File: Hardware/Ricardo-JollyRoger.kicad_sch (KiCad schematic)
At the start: 46 parts, among them J1 RBUS, J3 Conn_01x08_Pin, U1 ESP32-S3, U7 LM66200DRLR, Y1 R940000171

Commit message: Updated footprints
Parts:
- 12VLED1, 3V3LED1, CRXLED1, CTXLED1, TXLED1: footprint Resistor_SMD:R_0402_1005Metric -> LED_SMD:LED_0402_1005Metric
- U7: footprint SOTFL50P160X60-8N -> iclr:SOTFL50P160X60-8N
- Y1: footprint Crystal:Crystal_SMD_2016-4Pin_2.0x1.6mm -> iclr:Crystal_SMD_2016-4Pin_2.0x1.6mm
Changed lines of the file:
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@@
 			)
 		)
-		(property "Footprint" "Resistor_SMD:R_0402_1005Metric"
+		(property "Footprint" "LED_SMD:LED_0402_1005Metric"
 			(at 25.4 21.59 90)
 			(effects
@@
 			)
 		)
-		(property "Footprint" "Resistor_SMD:R_0402_1005Metric"
+		(property "Footprint" "LED_SMD:LED_0402_1005Metric"
 			(at 54.61 21.59 90)
 			(effects
@@
 			)
 		)
-		(property "Footprint" "Resistor_SMD:R_0402_1005Metric"
+		(property "Footprint" "LED_SMD:LED_0402_1005Metric"
 			(at 63.5 26.67 90)
 			(effects
@@
 			)
 		)
-		(property "Footprint" "Resistor_SMD:R_0402_1005Metric"
+		(property "Footprint" "LED_SMD:LED_0402_1005Metric"
 			(at 25.4 30.48 90)
 			(effects
@@
 			)
 		)
-		(property "Footprint" "Resistor_SMD:R_0402_1005Metric"
+		(property "Footprint" "LED_SMD:LED_0402_1005Metric"
 			(at 25.4 40.64 90)
 			(effects
@@
 			)
 		)
-		(property "Footprint" "SOTFL50P160X60-8N"
+		(property "Footprint" "iclr:SOTFL50P160X60-8N"
 			(at 232.41 53.34 0)
 			(effects
@@
 			)
 		)
-		(property "Footprint" "Crystal:Crystal_SMD_2016-4Pin_2.0x1.6mm"
+		(property "Footprint" "iclr:Crystal_SMD_2016-4Pin_2.0x1.6mm"
 			(at 156.21 132.08 0)
 			(effects
@@
 		)
 		(instances
-			(project "Ricardo-BlackBox"
+			(project "Ricardo-JollyRoger"
 				(path "/7db990e4-92e1-4f99-b4d2-435bbec1ba83"
 					(page "3")
@@
 		)
 		(instances
-			(project "Ricardo-BlackBox"
+			(project "Ricardo-JollyRoger"
 				(path "/7db990e4-92e1-4f99-b4d2-435bbec1ba83"
 					(page "2")
@@
 		)
 		(instances
-			(project "Ricardo-BlackBox"
+			(project "Ricardo-JollyRoger"
 				(path "/7db990e4-92e1-4f99-b4d2-435bbec1ba83"
 					(page "4")

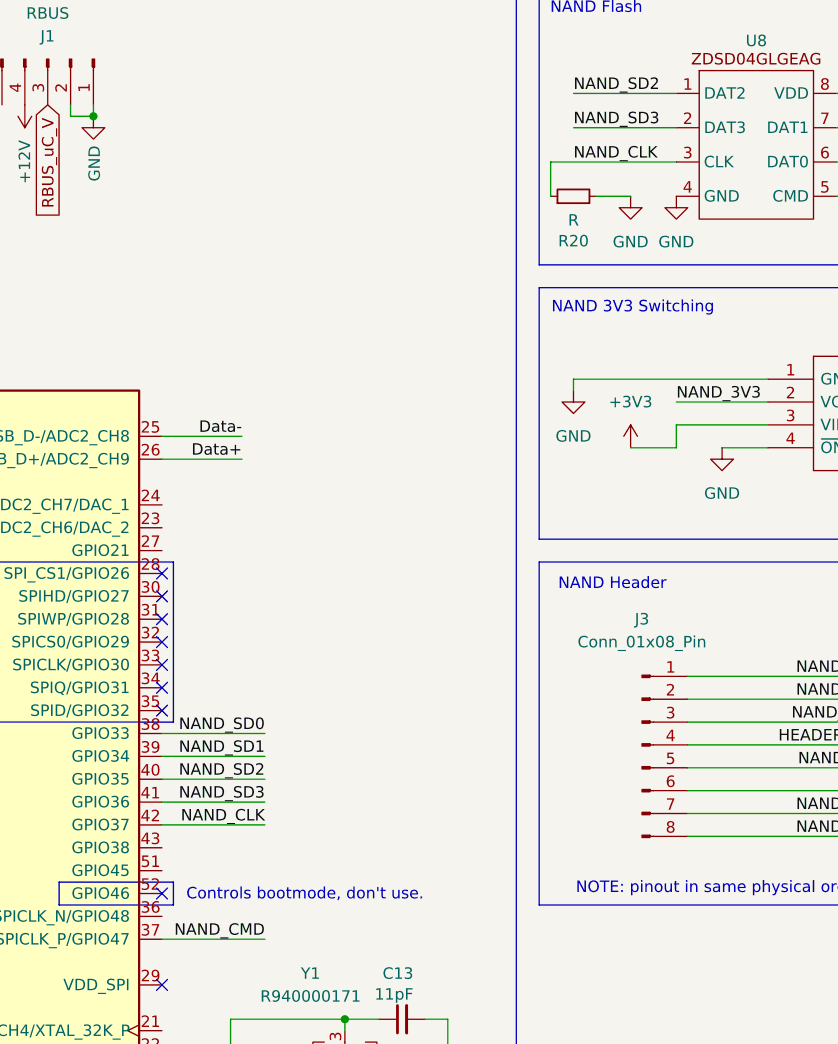
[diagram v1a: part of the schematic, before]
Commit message: Updated NAND termination resistor
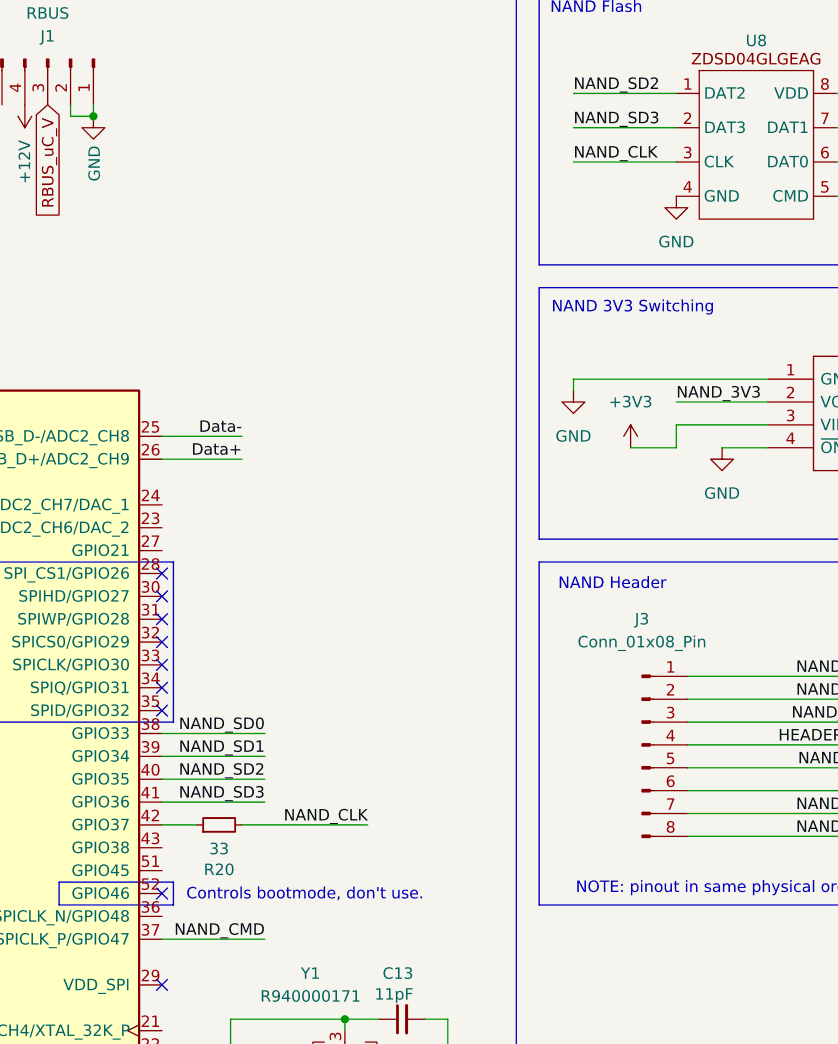
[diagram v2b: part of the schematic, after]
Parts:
- R20: value R -> 33
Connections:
- net GND: no longer R20.2
- net NAND_CLK: now also R20.2; no longer R20.1, U1.42 (GPIO37)
- new net: R20.1, U1.42 (GPIO37)
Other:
- moved on the sheet: R20
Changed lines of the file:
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@@
 	(wire
 		(pts
-			(xy 135.89 105.41) (xy 147.32 105.41)
-		)
-		(stroke
-			(width 0)
-			(type default)
-		)
-	)
-	(wire
-		(pts
 			(xy 236.22 60.96) (xy 246.38 60.96)
 		)
@@
 		)
 	)
+	(wire
+		(pts
+			(xy 135.89 105.41) (xy 139.7 105.41)
+		)
+		(stroke
+			(width 0)
+			(type default)
+		)
+	)
 	(polyline
 		(pts
@@
 	(wire
 		(pts
-			(xy 179.07 31.75) (xy 193.04 31.75)
-		)
-		(stroke
-			(width 0)
-			(type default)
-		)
-	)
-	(wire
-		(pts
 			(xy 55.88 165.1) (xy 63.5 165.1)
 		)
@@
 	(wire
 		(pts
-			(xy 184.15 35.56) (xy 187.96 35.56)
+			(xy 125.73 25.4) (xy 125.73 26.67)
 		)
 		(stroke
@@
 	(wire
 		(pts
-			(xy 125.73 25.4) (xy 125.73 26.67)
+			(xy 25.4 191.77) (xy 30.48 191.77)
 		)
 		(stroke
@@
 	(wire
 		(pts
-			(xy 25.4 191.77) (xy 30.48 191.77)
+			(xy 273.05 33.02) (xy 270.51 33.02)
 		)
 		(stroke
@@
 	(wire
 		(pts
-			(xy 273.05 33.02) (xy 270.51 33.02)
+			(xy 135.89 135.89) (xy 143.51 135.89)
 		)
 		(stroke
@@
 	(wire
 		(pts
-			(xy 135.89 135.89) (xy 143.51 135.89)
+			(xy 45.72 170.18) (xy 45.72 171.45)
 		)
 		(stroke
@@
 	(wire
 		(pts
-			(xy 45.72 170.18) (xy 45.72 171.45)
+			(xy 181.61 31.75) (xy 193.04 31.75)
 		)
 		(stroke
@@
 	(wire
 		(pts
-			(xy 179.07 35.56) (xy 179.07 31.75)
-		)
-		(stroke
-			(width 0)
-			(type default)
-		)
-	)
-	(wire
-		(pts
 			(xy 34.29 170.18) (xy 34.29 165.1)
 		)
@@
 	(wire
 		(pts
+			(xy 144.78 105.41) (xy 158.75 105.41)
+		)
+		(stroke
+			(width 0)
+			(type default)
+		)
+	)
+	(wire
+		(pts
 			(xy 135.89 118.11) (xy 147.32 118.11)
 		)
@@
 	)
 	(label "NAND_CLK"
-		(at 147.32 105.41 180)
+		(at 158.75 105.41 180)
 		(fields_autoplaced yes)
 		(effects
@@
 	(symbol
 		(lib_id "Device:R_Small")
-		(at 181.61 35.56 90)
+		(at 142.24 105.41 90)
 		(unit 1)
 		(exclude_from_sim no)
@@
 		(dnp no)
 		(property "Reference" "R20"
-			(at 181.61 40.5384 90)
+			(at 142.24 110.3884 90)
 			(effects
 				(font
@@
 			)
 		)
-		(property "Value" "R"
-			(at 181.61 38.227 90)
+		(property "Value" "33"
+			(at 142.24 108.077 90)
 			(effects
 				(font
@@
 		)
 		(property "Footprint" "Resistor_SMD:R_0402_1005Metric"
-			(at 181.61 35.56 0)
+			(at 142.24 105.41 0)
 			(effects
 				(font
@@
 		)
 		(property "Datasheet" "~"
-			(at 181.61 35.56 0)
+			(at 142.24 105.41 0)
 			(effects
 				(font
@@
 		)
 		(property "Description" "Resistor, small symbol"
-			(at 181.61 35.56 0)
+			(at 142.24 105.41 0)
 			(effects
 				(font
@@
 					(unit 1)
 				)
-			)
-		)
-	)
-	(symbol
-		(lib_id "power:GND")
-		(at 187.96 35.56 0)
-		(unit 1)
-		(exclude_from_sim no)
-		(in_bom yes)
-		(on_board yes)
-		(dnp no)
-		(fields_autoplaced yes)
-		(property "Reference" "#PWR056"
-			(at 187.96 41.91 0)
-			(effects
-				(font
-					(size 1.27 1.27)
-				)
-				(hide yes)
-			)
-		)
-		(property "Value" "GND"
-			(at 187.96 40.64 0)
-			(effects
-				(font
-					(size 1.27 1.27)
-				)
-			)
-		)
-		(property "Footprint" ""
-			(at 187.96 35.56 0)
-			(effects
-				(font
-					(size 1.27 1.27)
-				)
-				(hide yes)
-			)
-		)
-		(property "Datasheet" ""
-			(at 187.96 35.56 0)
-			(effects
-				(font
-					(size 1.27 1.27)
-				)
-				(hide yes)
-			)
-		)
-		(property "Description" "Power symbol creates a global label with name \"GND\" , ground"
-			(at 187.96 35.56 0)
-			(effects
-				(font
-					(size 1.27 1.27)
-				)
-				(hide yes)
-			)
-		)
-		(pin "1"
-		)
-		(instances
-			(project "Ricardo-BlackBox"
-				(path "/7db990e4-92e1-4f99-b4d2-435bbec1ba83"
-					(reference "#PWR056")
-					(unit 1)
-				)
